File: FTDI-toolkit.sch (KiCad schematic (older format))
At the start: 88 parts, among them IC1 TLV70033DCKT, IC12 SN74LV1T125DCKR, IC13 74HC00BQ, IC15 TS5A3359, IC2 TLV70018DCKT, IC3 TS5A3359, IC7 SN74LV1T125DCKR, U1 FT2232HQ, Y1 MQ-6.000-12-30/30/

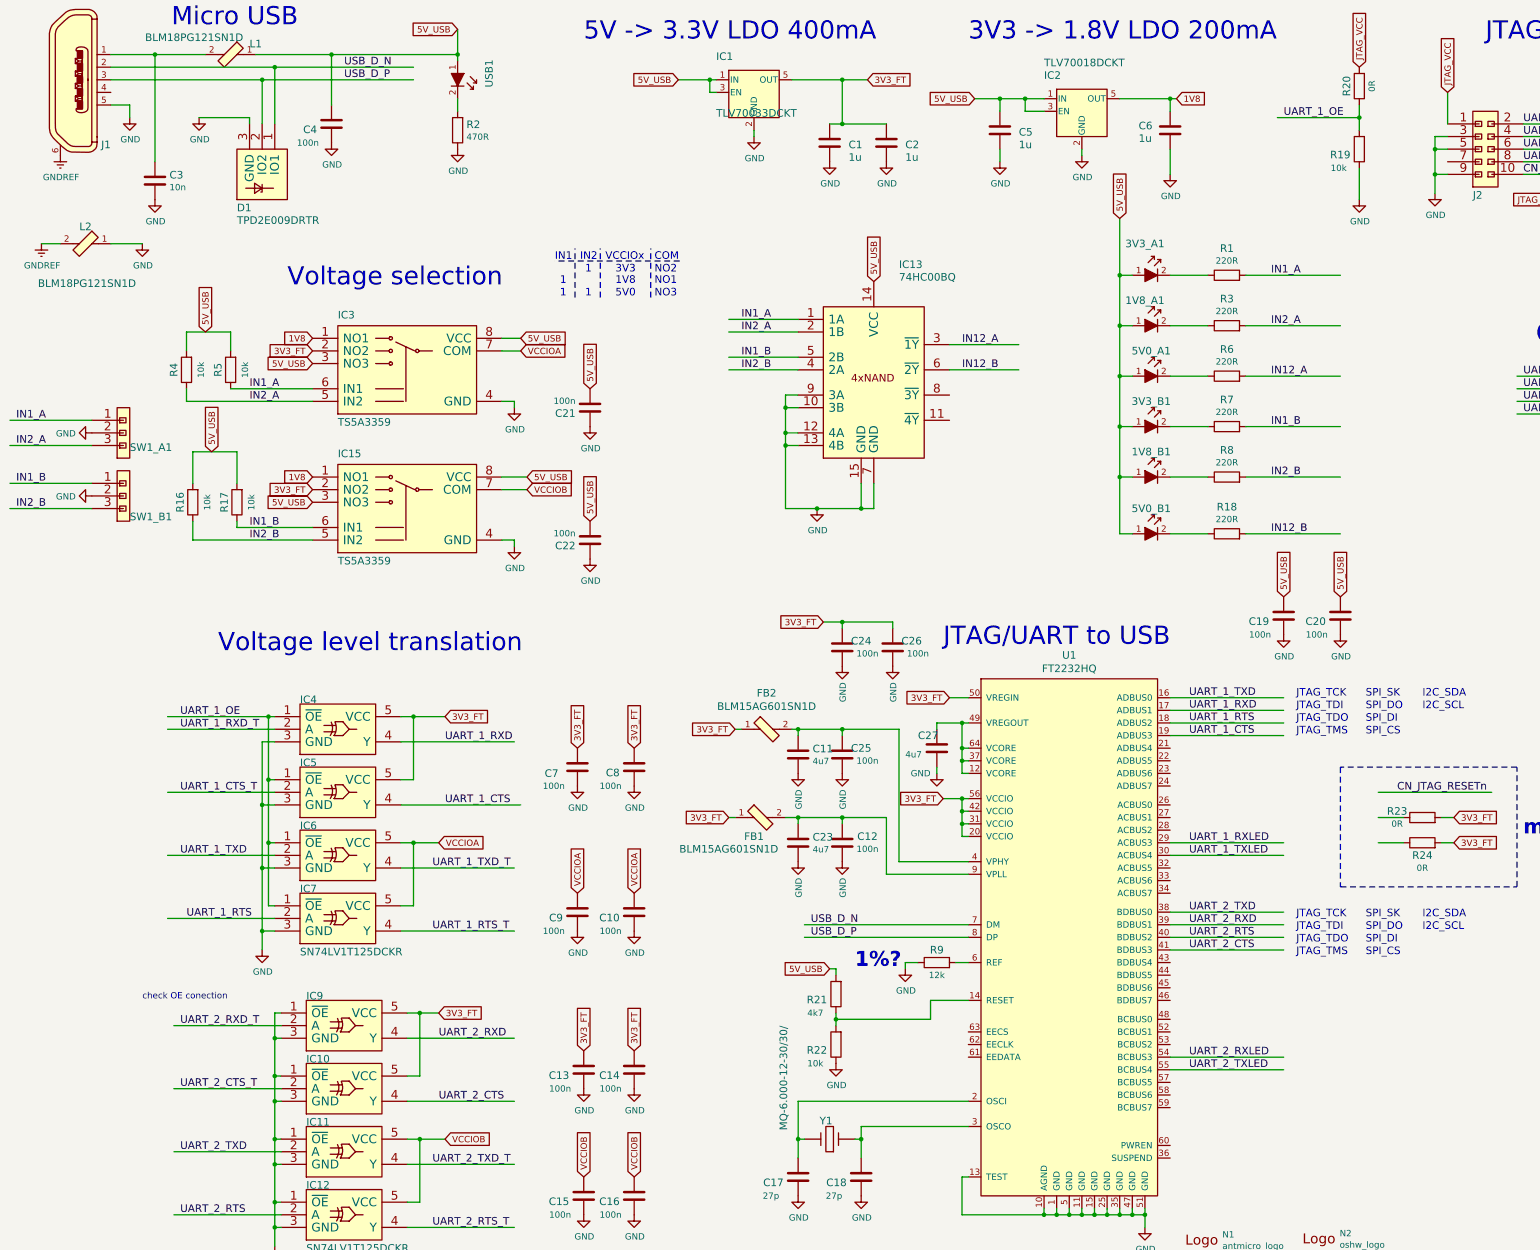
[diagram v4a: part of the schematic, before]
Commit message: Finish routing, DRC-clean
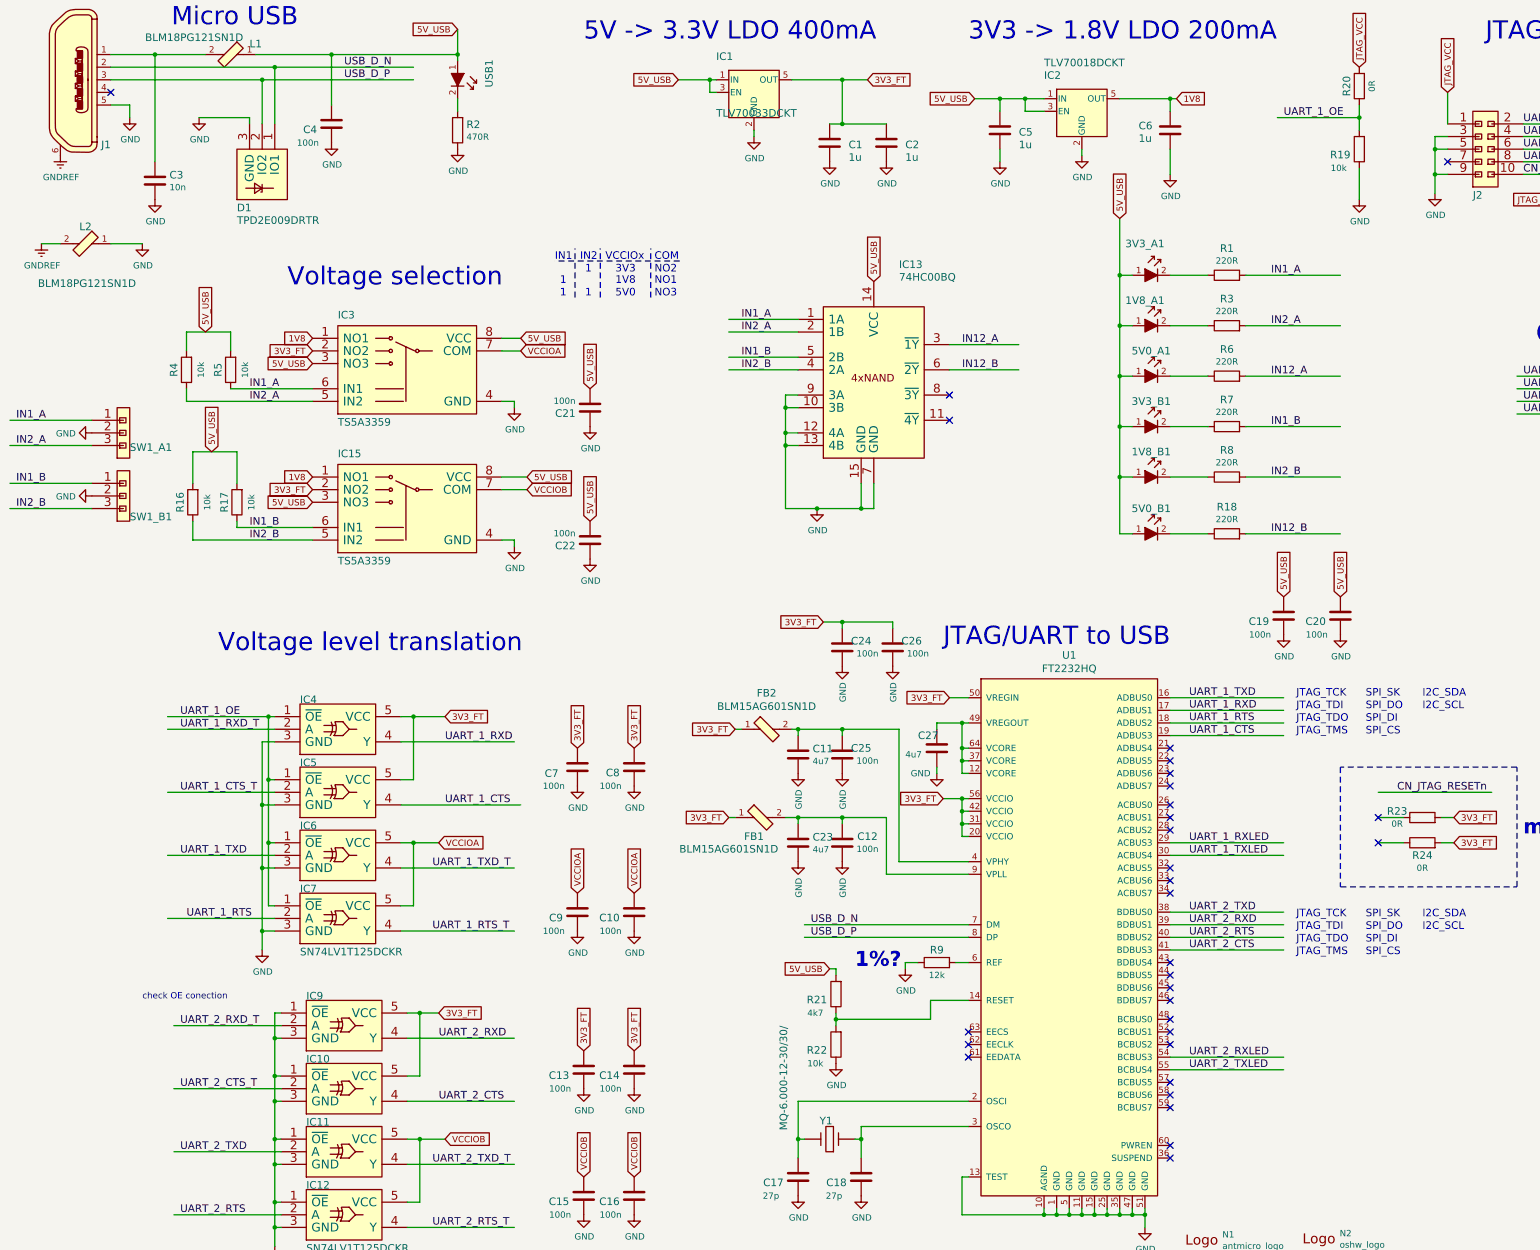
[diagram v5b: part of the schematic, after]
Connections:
- no-connect marks 0 -> 31
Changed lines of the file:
@@
 Wire Wire Line
 	1500 3000 1750 3000
-Wire Wire Line
-	1100 3000 950  3000
 Text GLabel 5300 4150 1    50   Input ~ 0
 5V_USB
@@
 	9200 2250 9200 2300
 Wire Wire Line
-	8750 1850 8900 1850
-Connection ~ 8750 1850
-Wire Wire Line
 	8900 1950 8750 1950
 Wire Wire Line
@@
 Wire Wire Line
 	7750 6850 7750 7900
-Wire Wire Line
-	7750 7900 8300 7900
 Connection ~ 7300 6850
 Wire Wire Line
@@
 Wire Wire Line
 	7650 7550 7650 8000
-Wire Wire Line
-	7650 8000 8300 8000
 Connection ~ 7300 7550
 Text GLabel 8150 6600 0    50   Input ~ 0
@@
 Text Notes 11900 8450 0    60   ~ 0
 I2C_SCL
+NoConn ~ 9900 7000
+NoConn ~ 9900 7100
+NoConn ~ 9900 7200
+NoConn ~ 9900 7300
+NoConn ~ 9900 7450
+NoConn ~ 9900 7550
+NoConn ~ 9900 7650
+NoConn ~ 9900 7950
+NoConn ~ 9900 8050
+NoConn ~ 9900 8150
+NoConn ~ 9900 8700
+NoConn ~ 9900 8800
+NoConn ~ 9900 8900
+NoConn ~ 9900 9000
+NoConn ~ 9900 9150
+NoConn ~ 9900 9250
+NoConn ~ 9900 9350
+NoConn ~ 8300 9250
+NoConn ~ 8300 9350
+NoConn ~ 8300 9450
+NoConn ~ 9900 9650
+NoConn ~ 9900 9750
+NoConn ~ 9900 9850
+NoConn ~ 9900 10150
+NoConn ~ 9900 10250
+Wire Wire Line
+	7750 7900 8300 7900
+Wire Wire Line
+	7650 8000 8300 8000
+Wire Wire Line
+	950  3000 1100 3000
+Wire Wire Line
+	8750 1850 8900 1850
+Connection ~ 8750 1850
+NoConn ~ 12100 2350
+NoConn ~ 1500 1800
+NoConn ~ 8150 4400
+NoConn ~ 11550 7550
+NoConn ~ 11550 7750
+NoConn ~ 8150 4200
 $EndSCHEMATC

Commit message: Replace LDO
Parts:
- IC1: footprint Package_TO_SOT_SMD:SOT-353_SC-70-5 -> antmicro-footprints:SC-70-5; symbol Regulator_Linear:TLV70033_SOT353 -> antmicroPMICVoltageRegulatorsLinear:TLV700
- IC2: footprint Package_TO_SOT_SMD:SOT-353_SC-70-5 -> antmicro-footprints:SC-70-5; symbol Regulator_Linear:TLV70018_SOT353 -> antmicroPMICVoltageRegulatorsLinear:TLV700
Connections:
- wire segments 326 -> 328
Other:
- moved on the sheet: C6, IC1, IC2
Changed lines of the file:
@@
 Wire Wire Line
 	8550 2250 8550 2350
-Text GLabel 9950 1850 2    50   Input ~ 0
+Text GLabel 10150 1850 2    50   Input ~ 0
 1V8
 Wire Wire Line
-	9500 1850 9900 1850
-Wire Wire Line
-	9900 1850 9900 1950
-Connection ~ 9900 1850
-Wire Wire Line
-	9900 1850 9950 1850
-Wire Wire Line
-	9900 2250 9900 2450
-Text GLabel 6000 1700 0    50   Input ~ 0
+	9700 1850 10100 1850
+Wire Wire Line
+	10100 1850 10100 1950
+Connection ~ 10100 1850
+Wire Wire Line
+	10100 1850 10150 1850
+Wire Wire Line
+	10100 2250 10100 2450
+Text GLabel 5650 1700 0    50   Input ~ 0
 5V_USB
-Wire Wire Line
-	6000 1700 6250 1700
-Wire Wire Line
-	6250 1700 6250 1800
-Wire Wire Line
-	6250 1800 6300 1800
-Wire Wire Line
-	6250 1700 6300 1700
-Connection ~ 6250 1700
 Text GLabel 7500 1700 2    50   Input ~ 0
 3V3_FT
@@
 Review connections!!!!
 Wire Wire Line
-	8750 1850 8750 1950
-Wire Wire Line
 	1500 1900 1650 1900
 Wire Wire Line
@@
 	4250 1850 4250 1950
 Wire Wire Line
-	6600 2100 6600 2150
-Wire Wire Line
-	9200 2250 9200 2300
-Wire Wire Line
-	8900 1950 8750 1950
-Wire Wire Line
 	8550 1950 8550 1850
-Connection ~ 8550 1850
-Wire Wire Line
-	8550 1850 8750 1850
 Wire Wire Line
 	14050 2750 14050 2700
@@
 	14550 2700 14550 3050
 Connection ~ 14150 2700
-$Comp
-L Regulator_Linear:TLV70033_SOT353 IC1
-U 1 1 5E5F7C27
-P 6600 1800
-F 0 "IC1" H 6300 2050 60  0000 L BNN
-F 1 "TLV70033DCKT" H 6300 1600 60  0000 L BNN
-F 2 "Package_TO_SOT_SMD:SOT-353_SC-70-5" H 6300 1600 60  0001 C CNN
-F 3 "" H 6300 1600 60  0000 C CNN
-	1    6600 1800
-	1    0    0    -1
-$EndComp
 $Comp
 L antmicroFerriteBeadsandChips:BLM18PG121SN1D L2
@@
 L power:GND #PWR0130
 U 1 1 5E8E0D0B
-P 6600 2150
-F 0 "#PWR0130" H 6600 1900 50  0001 C CNN
-F 1 "GND" H 6605 1977 50  0000 C CNN
-F 2 "" H 6600 2150 50  0001 C CNN
-F 3 "" H 6600 2150 50  0001 C CNN
-	1    6600 2150
+P 6950 1900
+F 0 "#PWR0130" H 6950 1650 50  0001 C CNN
+F 1 "GND" H 6955 1727 50  0000 C CNN
+F 2 "" H 6950 1900 50  0001 C CNN
+F 3 "" H 6950 1900 50  0001 C CNN
+	1    6950 1900
 	1    0    0    -1
 $EndComp
@@
 L power:GND #PWR0129
 U 1 1 5E804EDC
-P 9900 2450
-F 0 "#PWR0129" H 9900 2200 50  0001 C CNN
-F 1 "GND" H 9905 2277 50  0000 C CNN
-F 2 "" H 9900 2450 50  0001 C CNN
-F 3 "" H 9900 2450 50  0001 C CNN
-	1    9900 2450
+P 10100 2450
+F 0 "#PWR0129" H 10100 2200 50  0001 C CNN
+F 1 "GND" H 10105 2277 50  0000 C CNN
+F 2 "" H 10100 2450 50  0001 C CNN
+F 3 "" H 10100 2450 50  0001 C CNN
+	1    10100 2450
 	1    0    0    -1
 $EndComp
@@
 L power:GND #PWR0128
 U 1 1 5E7C4348
-P 9200 2300
-F 0 "#PWR0128" H 9200 2050 50  0001 C CNN
-F 1 "GND" H 9205 2127 50  0000 C CNN
-F 2 "" H 9200 2300 50  0001 C CNN
-F 3 "" H 9200 2300 50  0001 C CNN
-	1    9200 2300
+P 9750 2050
+F 0 "#PWR0128" H 9750 1800 50  0001 C CNN
+F 1 "GND" H 9755 1877 50  0000 C CNN
+F 2 "" H 9750 2050 50  0001 C CNN
+F 3 "" H 9750 2050 50  0001 C CNN
+	1    9750 2050
 	1    0    0    -1
 $EndComp
@@
 L antmicroCapacitors0603:C_1u_0603 C6
 U 1 1 5E780C9B
-P 9900 2100
-F 0 "C6" H 10150 2100 60  0000 R TNN
-F 1 "1u" H 10150 2200 60  0000 R TNN
-F 2 "antmicro-footprints:0603-cap" H 9700 2000 60  0001 C CNN
-F 3 "" H 9700 2000 60  0000 C CNN
-F 4 "0603YD105KAT2A" H 0   0   50  0001 C CNN "MPN"
-F 5 "WALSIN" H 0   0   50  0001 C CNN "Manufacturer"
-F 6 "1u" H 0   0   50  0001 C CNN "Val"
-	1    9900 2100
+P 10100 2100
+F 0 "C6" H 10350 2100 60  0000 R TNN
+F 1 "1u" H 10350 2200 60  0000 R TNN
+F 2 "antmicro-footprints:0603-cap" H 9900 2000 60  0001 C CNN
+F 3 "" H 9900 2000 60  0000 C CNN
+F 4 "0603YD105KAT2A" H 200 0   50  0001 C CNN "MPN"
+F 5 "WALSIN" H 200 0   50  0001 C CNN "Manufacturer"
+F 6 "1u" H 200 0   50  0001 C CNN "Val"
+	1    10100 2100
 	-1   0    0    1
 $EndComp
@@
 	1    8550 2100
 	-1   0    0    1
-$EndComp
-$Comp
-L Regulator_Linear:TLV70018_SOT353 IC2
-U 1 1 5E5F7C4B
-P 9200 1950
-F 0 "IC2" H 8900 2200 60  0000 L BNN
-F 1 "TLV70018DCKT" H 8900 2300 60  0000 L BNN
-F 2 "Package_TO_SOT_SMD:SOT-353_SC-70-5" H 8900 2250 60  0001 C CNN
-F 3 "" H 8900 2250 60  0000 C CNN
-	1    9200 1950
-	1    0    0    -1
 $EndComp
 $Comp
@@
 Wire Wire Line
 	950  3000 1100 3000
-Wire Wire Line
-	8750 1850 8900 1850
-Connection ~ 8750 1850
 NoConn ~ 12100 2350
 NoConn ~ 1500 1800
@@
 NoConn ~ 11550 7750
 NoConn ~ 8150 4200
+$Comp
+L antmicroPMICVoltageRegulatorsLinear:TLV700 IC2
+U 1 1 5E5F7C4B
+P 9200 1950
+F 0 "IC2" H 8900 2200 60  0000 L BNN
+F 1 "TLV70018DCKT" H 8900 2300 60  0000 L BNN
+F 2 "antmicro-footprints:SC-70-5" H 8900 2250 60  0001 C CNN
+F 3 "" H 8900 2250 60  0000 C CNN
+	1    9200 1950
+	1    0    0    -1
+$EndComp
+Wire Wire Line
+	6900 1800 6950 1800
+Wire Wire Line
+	6950 1800 6950 1900
+$Comp
+L antmicroPMICVoltageRegulatorsLinear:TLV700 IC1
+U 1 1 5E5F7C27
+P 6400 1800
+F 0 "IC1" H 6100 2050 60  0000 L BNN
+F 1 "TLV70033DCKT" H 6100 1600 60  0000 L BNN
+F 2 "antmicro-footprints:SC-70-5" H 6100 1600 60  0001 C CNN
+F 3 "" H 6100 1600 60  0000 C CNN
+	1    6400 1800
+	1    0    0    -1
+$EndComp
+Wire Wire Line
+	5650 1700 5850 1700
+Wire Wire Line
+	5850 1700 5850 1800
+Wire Wire Line
+	5850 1800 5900 1800
+Wire Wire Line
+	5900 1700 5850 1700
+Connection ~ 5850 1700
+Wire Wire Line
+	9700 1950 9750 1950
+Wire Wire Line
+	9750 1950 9750 2050
+Wire Wire Line
+	8550 1850 8650 1850
+Connection ~ 8550 1850
+Wire Wire Line
+	8700 1950 8650 1950
+Wire Wire Line
+	8650 1950 8650 1850
+Connection ~ 8650 1850
+Wire Wire Line
+	8650 1850 8700 1850
 $EndSCHEMATC

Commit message: Update component description and naming
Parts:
- removed R23, R24: R_0R_0402, antmicro-footprints:0402-res, symbol antmicroResistors0402:R_0R_0402
- R9: value R_12k_0402 -> R_12k_0402_1%
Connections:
- net labels added: ADBUS0, ADBUS1, ADBUS2, ADBUS3, BDBUS0, BDBUS1, BDBUS2, BDBUS3
- net labels removed: UART_1_CTS, UART_1_RTS, UART_1_RXD, UART_1_TXD, UART_2_CTS, UART_2_RTS, UART_2_RXD, UART_2_TXD
- wire segments 328 -> 323
- no-connect marks 31 -> 29
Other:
- note added: "1.1.0 07/2020\n"
- note added: "https://dev.antmicro.com/git/antmicro-ftdi-toolkit-hw"
- note removed: "1%?\n"
- note removed: "1.1.0 07.2020"
- note removed: "misc redundant?\n"
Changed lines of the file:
@@
 Text Notes 12800 3800 0    144  ~ 0
 Goldpin connector
-Text Label 10050 6700 0    60   ~ 0
-UART_1_RXD
-Text Label 10050 6600 0    60   ~ 0
-UART_1_TXD
 Text Label 10050 8400 0    60   ~ 0
-UART_2_RXD
+BDBUS1
 Text Label 10050 8300 0    60   ~ 0
-UART_2_TXD
+BDBUS0
 Text Notes 8300 1400 0    144  ~ 0
 3V3 -> 1.8V LDO 200mA
 Text Label 10050 6900 0    60   ~ 0
-UART_1_CTS
+ADBUS3
 Text Label 10050 6800 0    60   ~ 0
-UART_1_RTS
+ADBUS2
 Text Label 10050 8600 0    60   ~ 0
-UART_2_CTS
+BDBUS3
 Text Label 10050 8500 0    60   ~ 0
-UART_2_RTS
+BDBUS2
 Text Label 10050 7750 0    60   ~ 0
 UART_1_RXLED
@@
 Text Notes 2350 6250 0    144  ~ 0
 Voltage level translation
-Text Label 4150 6950 0    60   ~ 0
-UART_1_RXD
 Text Label 4150 7450 0    60   ~ 0
-UART_1_CTS
-Text Label 2050 7850 0    60   ~ 0
-UART_1_TXD
+ADBUS3
 Text Label 2100 8350 0    60   ~ 0
-UART_1_RTS
+ADBUS2
 Text Label 2050 6850 0    60   ~ 0
 UART_1_RXD_T
@@
 CN_JTAG_RESETn
 Text Label 12700 2050 0    60   ~ 0
-UART_1_CTS
+ADBUS3
 Text Label 12700 2150 0    60   ~ 0
-UART_1_TXD
+ADBUS0
 Text Label 12700 2250 0    60   ~ 0
-UART_1_RTS
+ADBUS2
 Text Label 12700 2350 0    60   ~ 0
-UART_1_RXD
+ADBUS1
 Text Notes 10900 6600 0    60   ~ 0
 JTAG_TCK
@@
 UART_2_CTS_T
 Text Label 2050 10700 0    60   ~ 0
-UART_2_RTS
+BDBUS2
 Text Label 2050 10200 0    60   ~ 0
-UART_2_TXD
+BDBUS0
 Text Label 4050 7950 0    60   ~ 0
 UART_1_TXD_T
@@
 	8700 4000 8150 4000
 Text Label 4100 9300 0    60   ~ 0
-UART_2_RXD
+BDBUS1
 Text Label 4100 9800 0    60   ~ 0
-UART_2_CTS
+BDBUS3
 Wire Wire Line
 	3850 9100 3950 9100
@@
 Wire Wire Line
 	6850 4600 6850 5100
-Text Notes 15450 11050 0    47   ~ 0
-1.1.0 07.2020
 Connection ~ 7100 5100
 Wire Wire Line
@@
 U 1 1 5F5D3CC5
 P 7300 7750
-F 0 "C12" H 7500 7800 60  0000 C CNN
+F 0 "C12" H 7450 7850 60  0000 C CNN
 F 1 "C_100n_0402_16V" H 7300 7600 60  0001 C CNN
 F 2 "antmicro-footprints:0402-cap" H 7500 7950 60  0001 L CNN
@@
 F 4 "MULTICOMP" H 7500 8150 60  0001 L CNN "Manufacturer"
 F 5 "MC0402B104K160CT" H 7500 8050 60  0001 L CNN "MPN"
-F 6 "100n" H 7500 7700 50  0000 C CNN "Val"
+F 6 "100n" H 7500 7750 50  0000 C CNN "Val"
 	1    7300 7750
 	1    0    0    -1
@@
 U 1 1 5FC7C451
 P 7300 7050
-F 0 "C25" H 7450 7100 60  0000 C CNN
+F 0 "C25" H 7500 7100 60  0000 C CNN
 F 1 "C_100n_0402_16V" H 7300 6900 60  0001 C CNN
 F 2 "antmicro-footprints:0402-cap" H 7500 7250 60  0001 L CNN
@@
 U 1 1 5FCAF724
 P 6950 7050
-F 0 "C11" H 7065 7095 60  0000 L CNN
+F 0 "C11" H 6650 7100 60  0000 L CNN
 F 1 "C_4u7_0402" H 6950 6900 60  0001 C CNN
 F 2 "antmicro-footprints:0402-cap" H 7150 7250 60  0001 L CNN
@@
 F 4 "MURATA" H 7150 7450 60  0001 L CNN "Manufacturer"
 F 5 "GRM155R61A475MEAAD" H 7150 7350 60  0001 L CNN "MPN"
-F 6 "4u7" H 7065 6997 50  0000 L CNN "Val"
+F 6 "4u7" H 6650 7000 50  0000 L CNN "Val"
 	1    6950 7050
 	1    0    0    -1
@@
 U 1 1 5FCB05D9
 P 6950 7750
-F 0 "C23" H 7065 7795 60  0000 L CNN
+F 0 "C23" H 7000 7850 60  0000 L CNN
 F 1 "C_4u7_0402" H 6950 7600 60  0001 C CNN
 F 2 "antmicro-footprints:0402-cap" H 7150 7950 60  0001 L CNN
@@
 F 4 "MURATA" H 7150 8150 60  0001 L CNN "Manufacturer"
 F 5 "GRM155R61A475MEAAD" H 7150 8050 60  0001 L CNN "MPN"
-F 6 "4u7" H 7065 7697 50  0000 L CNN "Val"
+F 6 "4u7" H 7050 7750 50  0000 L CNN "Val"
 	1    6950 7750
 	1    0    0    -1
@@
 U 1 1 5FFC3DD8
 P 8050 7000
-F 0 "C27" H 7900 7100 60  0000 L CNN
+F 0 "C27" H 7850 7100 60  0000 L CNN
 F 1 "C_4u7_0402" H 8050 6850 60  0001 C CNN
 F 2 "antmicro-footprints:0402-cap" H 8250 7200 60  0001 L CNN
@@
 F 4 "MURATA" H 8250 7400 60  0001 L CNN "Manufacturer"
 F 5 "GRM155R61A475MEAAD" H 8250 7300 60  0001 L CNN "MPN"
-F 6 "4u7" H 7800 6950 50  0000 L CNN "Val"
+F 6 "4u7" H 7800 7000 50  0000 L CNN "Val"
 	1    8050 7000
 	1    0    0    -1
@@
 P 8050 8700
 F 0 "R9" H 8050 8800 60  0000 C CNN
-F 1 "R_12k_0402" H 8050 8550 60  0001 C CNN
+F 1 "R_12k_0402_1%" H 8050 8550 60  0001 C CNN
 F 2 "antmicro-footprints:0402-res" H 8250 8900 60  0001 L CNN
 F 3 "" H 8050 8700 50  0001 C CNN
@@
 Wire Wire Line
 	7800 8700 7800 8750
-Text Notes 7400 8750 0    118  ~ 24
-1%?\n
 Wire Wire Line
 	7250 9100 7250 9150
@@
 U 1 1 60314ADF
 P 7300 6200
-F 0 "C24" H 7450 6250 60  0000 C CNN
+F 0 "C24" H 7500 6250 60  0000 C CNN
 F 1 "C_100n_0402_16V" H 7300 6050 60  0001 C CNN
 F 2 "antmicro-footprints:0402-cap" H 7500 6400 60  0001 L CNN
@@
 U 1 1 603158A4
 P 7700 6200
-F 0 "C26" H 7850 6250 60  0000 C CNN
+F 0 "C26" H 7900 6250 60  0000 C CNN
 F 1 "C_100n_0402_16V" H 7700 6050 60  0001 C CNN
 F 2 "antmicro-footprints:0402-cap" H 7900 6400 60  0001 L CNN
@@
 Wire Wire Line
 	9900 8600 10800 8600
-Wire Wire Line
-	11550 7350 12450 7350
-Text Label 11700 7350 0    60   ~ 0
-CN_JTAG_RESETn
-$Comp
-L antmicroResistors0402:R_0R_0402 R24
-U 1 1 5FA1BF2C
-P 11900 7750
-F 0 "R24" H 11900 7650 60  0000 C CNN
-F 1 "R_0R_0402" H 11900 7600 60  0001 C CNN
-F 2 "antmicro-footprints:0402-res" H 12100 7950 60  0001 L CNN
-F 3 "" H 11900 7750 50  0001 C CNN
-F 4 "PANASONIC" H 12100 8150 60  0001 L CNN "Manufacturer"
-F 5 "ERJ2GE0R00X" H 12100 8050 60  0001 L CNN "MPN"
-F 6 "0R" H 11900 7550 50  0000 C CNN "Val"
-	1    11900 7750
-	1    0    0    -1
-$EndComp
-Wire Wire Line
-	12050 7750 12150 7750
-Wire Wire Line
-	11750 7750 11550 7750
-Text GLabel 12150 7750 2    50   Input ~ 0
-3V3_FT
-$Comp
-L antmicroResistors0402:R_0R_0402 R23
-U 1 1 5F9305BF
-P 11900 7550
-F 0 "R23" H 11700 7600 60  0000 C CNN
-F 1 "R_0R_0402" H 11900 7400 60  0001 C CNN
-F 2 "antmicro-footprints:0402-res" H 12100 7750 60  0001 L CNN
-F 3 "" H 11900 7550 50  0001 C CNN
-F 4 "PANASONIC" H 12100 7950 60  0001 L CNN "Manufacturer"
-F 5 "ERJ2GE0R00X" H 12100 7850 60  0001 L CNN "MPN"
-F 6 "0R" H 11700 7500 50  0000 C CNN "Val"
-	1    11900 7550
-	1    0    0    -1
-$EndComp
-Wire Wire Line
-	12050 7550 12150 7550
-Wire Wire Line
-	11550 7550 11750 7550
-Text GLabel 12150 7550 2    50   Input ~ 0
-3V3_FT
-Wire Notes Line
-	11250 8100 12650 8100
-Wire Notes Line
-	12650 8100 12650 7150
-Wire Notes Line
-	12650 7150 11250 7150
-Wire Notes Line
-	11250 7150 11250 8100
-Text Notes 12700 7700 0    118  ~ 24
-misc redundant?\n
 Text Notes 11450 6600 0    60   ~ 0
 SPI_SK\n
@@
 NoConn ~ 1500 1800
 NoConn ~ 8150 4400
-NoConn ~ 11550 7550
-NoConn ~ 11550 7750
 NoConn ~ 8150 4200
 $Comp
@@
 Wire Wire Line
 	8650 1850 8700 1850
+Text Notes 15500 11050 0    39   ~ 0
+1.1.0 07/2020\n
+Text Notes 13400 10750 0    60   ~ 0
+https://dev.antmicro.com/git/antmicro-ftdi-toolkit-hw
+Text Label 4150 6950 0    60   ~ 0
+ADBUS1
+Text Label 10050 6700 0    60   ~ 0
+ADBUS1
+Text Label 2050 7850 0    60   ~ 0
+ADBUS0
+Text Label 10050 6600 0    60   ~ 0
+ADBUS0
 $EndSCHEMATC
